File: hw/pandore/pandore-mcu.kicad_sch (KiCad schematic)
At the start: 17 parts, among them U3 RP2350B, U5 mem_flash_spi

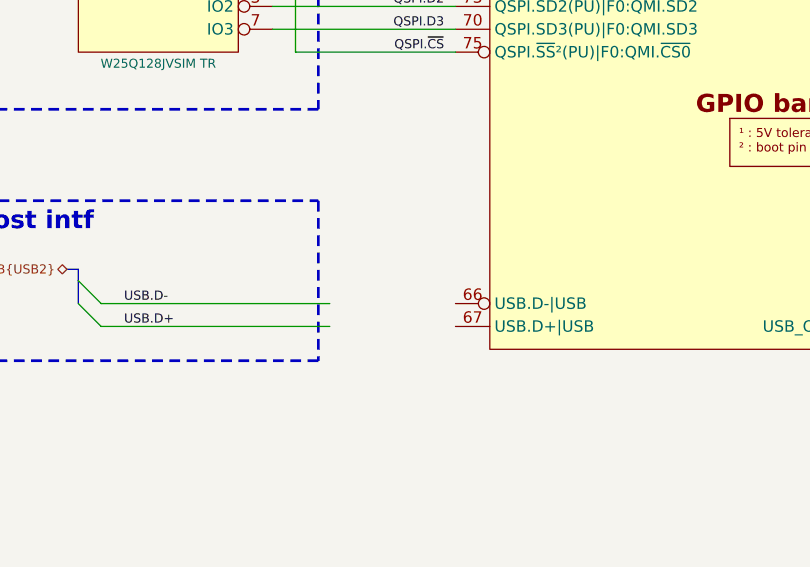
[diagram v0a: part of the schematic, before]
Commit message: added usb, hdmi and combo xlrtrs connectors resized pcb for something realistic (still wip)
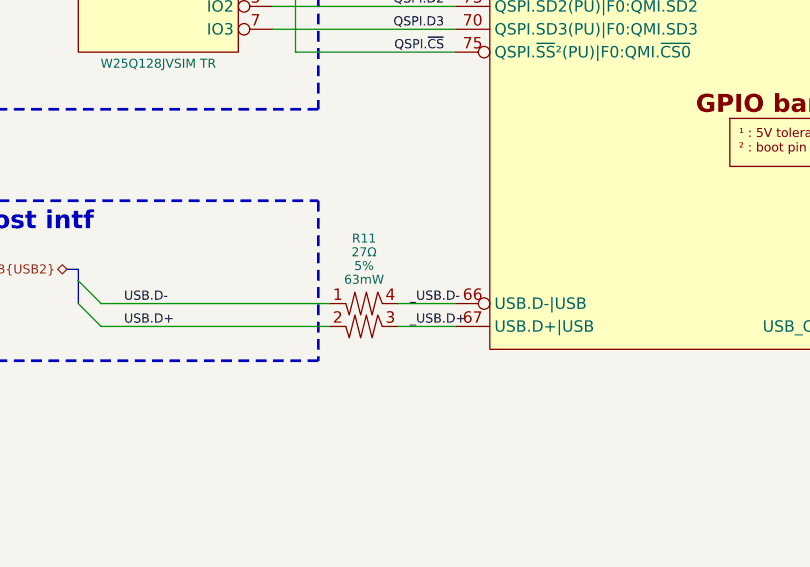
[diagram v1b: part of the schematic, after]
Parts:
- added R11: ${Resistance}, ${Tolerance}, ${Power}, reekilib_res:RESCAXSR65P100X100X35-4, symbol reekilib_res:res_2
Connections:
- net USB.D+: now also R11.2
- net USB.D-: now also R11.1
- net _USB.D-: now reaches U3.66 (USB.D-|USB)
- net _USB.D-: now also R11.4
- net _USB.D+: now reaches U3.67 (USB.D+|USB)
- net _USB.D+: now also R11.3

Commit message: added RP2350's crystals added 8p8c shielded with led connector (both the same for now)
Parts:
- added X1: ${F}, ${tol}+${stab}, ${load}, reekilib_osc:OSCCC320X250X90, symbol reekilib_xtl:crystal_shield
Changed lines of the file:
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@@
+	)
+	(symbol
+		(lib_id "reekilib_xtl:crystal_shield")
+		(at 142.24 43.18 0)
+		(unit 1)
+		(exclude_from_sim no)
+		(in_bom yes)
+		(on_board yes)
+		(dnp no)
+		(property "Reference" "X1"
+			(at 142.24 38.1 0)
+			(do_not_autoplace yes)
+			(effects
+				(font
+					(size 1 1)
+				)
+			)
+		)
+		(property "Value" "${F}, ${tol}+${stab}, ${load}"
+			(at 142.24 38.1 0)
+			(do_not_autoplace yes)
+			(effects
+				(font
+					(size 1 1)
+				)
+				(hide yes)
+			)
+		)
+		(property "Footprint" "reekilib_osc:OSCCC320X250X90"
+			(at 142.24 56.515 0)
+			(do_not_autoplace yes)
+			(effects
+				(font
+					(size 1 1)
+				)
+				(hide yes)
+			)
+		)
+		(property "Datasheet" "https://abracon.com/datasheets/ABM8-272-T3.pdf"
+			(at 142.24 58.42 0)
+			(do_not_autoplace yes)
+			(effects
+				(font
+					(size 1 1)
+				)
+				(hide yes)
+			)
+		)
+		(property "Description" "Crystal with shield"
+			(at 142.24 54.61 0)
+			(do_not_autoplace yes)
+			(effects
+				(font
+					(size 1 1)
+				)
+				(hide yes)
+			)
+		)
+		(property "F" "12MHz"
+			(at 140.97 50.165 0)
+			(do_not_autoplace yes)
+			(effects
+				(font
+					(size 1 1)
+				)
+				(justify right)
+			)
+		)
+		(property "tol" "30ppm"
+			(at 143.51 50.165 0)
+			(do_not_autoplace yes)
+			(effects
+				(font
+					(size 1 1)
+				)
+				(justify left)
+			)
+		)
+		(property "stab" "30ppm"
+			(at 150.495 50.165 0)
+			(do_not_autoplace yes)
+			(effects
+				(font
+					(size 1 1)
+				)
+				(justify left)
+				(hide yes)
+			)
+		)
+		(property "load" "10pF"
+			(at 142.24 52.07 0)
+			(do_not_autoplace yes)
+			(effects
+				(font
+					(size 1 1)
+				)
+			)
+		)
+		(property "MPN" "ABM8-272-T3"
+			(at 142.875 62.23 0)
+			(do_not_autoplace yes)
+			(effects
+				(font
+					(size 1 1)
+				)
+				(hide yes)
+			)
+		)
+		(property "MFG" "Abracon LLC"
+			(at 161.29 62.23 0)
+			(do_not_autoplace yes)
+			(effects
+				(font
+					(size 1 1)
+				)
+				(justify left)
+				(hide yes)
+			)
+		)
+		(property "Link" "https://abracon.com/search?q=ABM8-272-T3"
+			(at 196.215 62.23 0)
+			(do_not_autoplace yes)
+			(effects
+				(font
+					(size 1 1)
+				)
+				(justify left)
+				(hide yes)
+			)
+		)
+		(pin "1"
+		)
+		(pin "3"
+		)
+		(pin "2"
+		)
+		(pin "4"
+		)
+		(instances
+			(project ""
+				(path "/e55f2700-f75a-4062-8a27-fe258faa8966/57ec90ce-deb5-4a52-b1c0-0a997012959b/d2a190b7-8486-4aae-97c0-33ac8d90da8a"
+					(reference "X1")
+					(unit 1)
+				)
+				(path "/e55f2700-f75a-4062-8a27-fe258faa8966/f774142b-755f-468a-93e0-eecae9257f8f/8e05de8b-3536-4686-b4df-144081dee611"
+					(reference "X2")
+					(unit 1)
+				)
+			)
+		)
 	)
 	(symbol

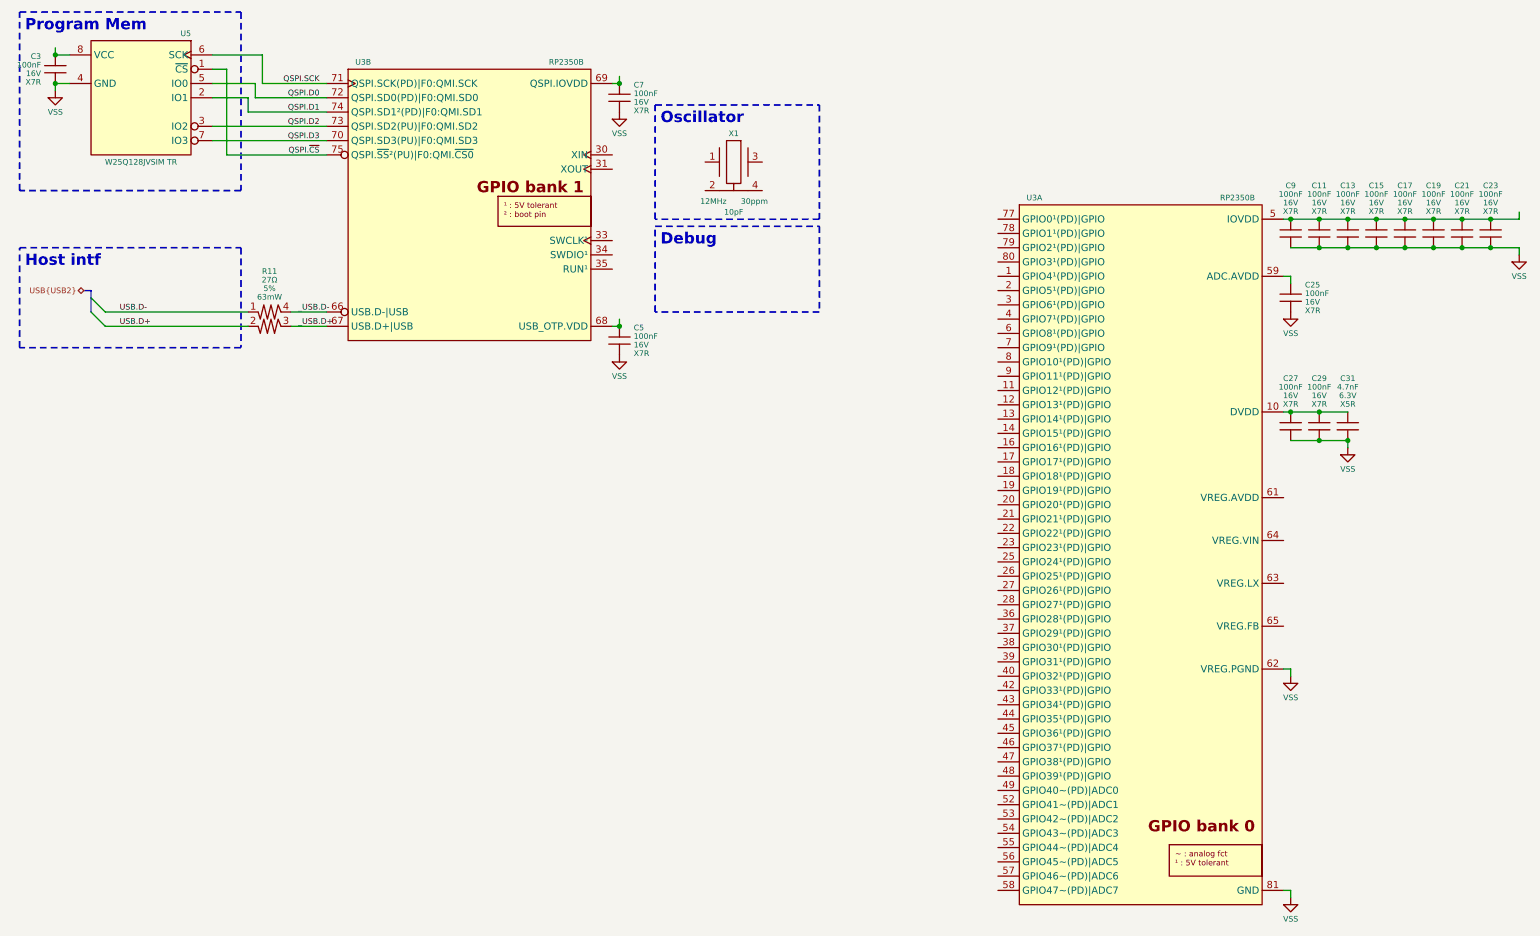
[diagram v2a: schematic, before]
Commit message: Added lots to sch and pcb: eth passive, audio codec, midi, teensy Corrected and added support for M.2
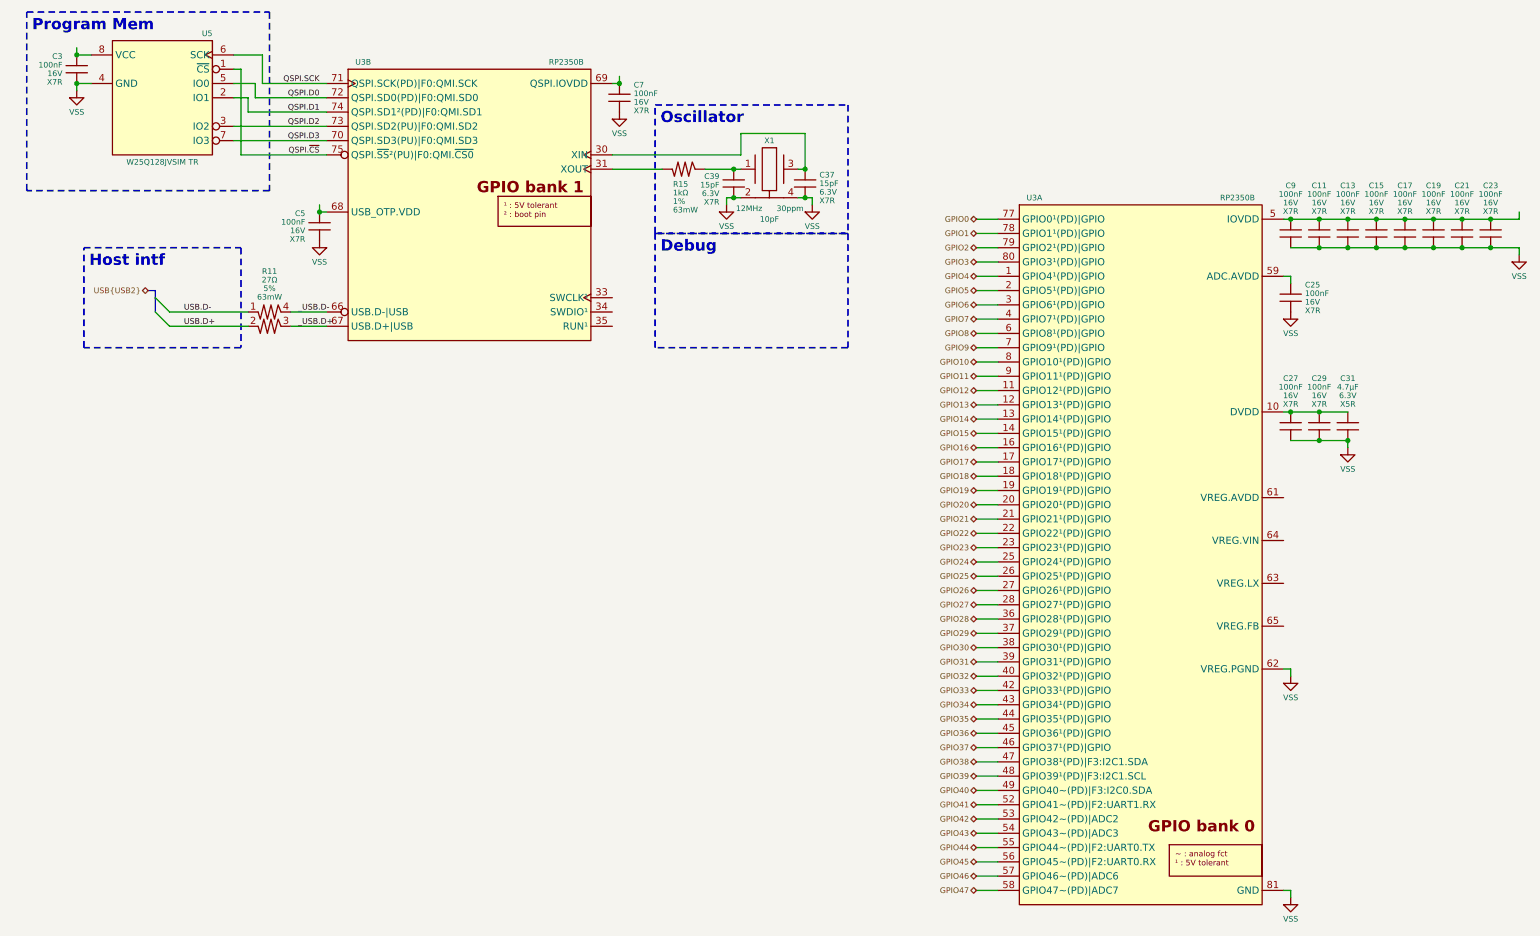
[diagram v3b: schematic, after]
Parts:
- added C37, C39: ${Capacitance}, ${Voltage}, ${Dielectric}, reekilib_cap:CAPC1005, symbol reekilib_cap:cap
- added R15: ${Resistance}, ${Tolerance}, ${Power}, reekilib_res:RESC1005, symbol reekilib_res:res
- C31: Capacitance 4.7nF -> 4.7µF
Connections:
- net VSS: now also X1.2, X1.4, C37.1, C39.1
- net GPIO4: now reaches U3.1 (GPIO4¹(PD)|GPIO)
- net GPIO12: now reaches U3.11 (GPIO12¹(PD)|GPIO)
- net GPIO13: now reaches U3.12 (GPIO13¹(PD)|GPIO)
- net GPIO14: now reaches U3.13 (GPIO14¹(PD)|GPIO)
- net GPIO15: now reaches U3.14 (GPIO15¹(PD)|GPIO)
- net GPIO16: now reaches U3.16 (GPIO16¹(PD)|GPIO)
- net GPIO17: now reaches U3.17 (GPIO17¹(PD)|GPIO)
- net GPIO18: now reaches U3.18 (GPIO18¹(PD)|GPIO)
- net GPIO19: now reaches U3.19 (GPIO19¹(PD)|GPIO)
- net GPIO5: now reaches U3.2 (GPIO5¹(PD)|GPIO)
- net GPIO20: now reaches U3.20 (GPIO20¹(PD)|GPIO)
- net GPIO21: now reaches U3.21 (GPIO21¹(PD)|GPIO)
- net GPIO22: now reaches U3.22 (GPIO22¹(PD)|GPIO)
- net GPIO23: now reaches U3.23 (GPIO23¹(PD)|GPIO)
- net GPIO24: now reaches U3.25 (GPIO24¹(PD)|GPIO)
- net GPIO25: now reaches U3.26 (GPIO25¹(PD)|GPIO)
- net GPIO26: now reaches U3.27 (GPIO26¹(PD)|GPIO)
- net GPIO27: now reaches U3.28 (GPIO27¹(PD)|GPIO)
- net GPIO6: now reaches U3.3 (GPIO6¹(PD)|GPIO)
- net GPIO28: now reaches U3.36 (GPIO28¹(PD)|GPIO)
- net GPIO29: now reaches U3.37 (GPIO29¹(PD)|GPIO)
- net GPIO30: now reaches U3.38 (GPIO30¹(PD)|GPIO)
- net GPIO31: now reaches U3.39 (GPIO31¹(PD)|GPIO)
- net GPIO7: now reaches U3.4 (GPIO7¹(PD)|GPIO)
- net GPIO32: now reaches U3.40 (GPIO32¹(PD)|GPIO)
- net GPIO33: now reaches U3.42 (GPIO33¹(PD)|GPIO)
- net GPIO34: now reaches U3.43 (GPIO34¹(PD)|GPIO)
- net GPIO35: now reaches U3.44 (GPIO35¹(PD)|GPIO)
- net GPIO36: now reaches U3.45 (GPIO36¹(PD)|GPIO)
- net GPIO37: now reaches U3.46 (GPIO37¹(PD)|GPIO)
- net GPIO38: now reaches U3.47 (GPIO38¹(PD)|GPIO)
- net GPIO39: now reaches U3.48 (GPIO39¹(PD)|GPIO)
- net GPIO40: now reaches U3.49 (GPIO40~(PD)|ADC0)
- net GPIO41: now reaches U3.52 (GPIO41~(PD)|ADC1)
- net GPIO42: now reaches U3.53 (GPIO42~(PD)|ADC2)
- net GPIO43: now reaches U3.54 (GPIO43~(PD)|ADC3)
- net GPIO44: now reaches U3.55 (GPIO44~(PD)|ADC4)
- net GPIO45: now reaches U3.56 (GPIO45~(PD)|ADC5)
- net GPIO46: now reaches U3.57 (GPIO46~(PD)|ADC6)
- net GPIO47: now reaches U3.58 (GPIO47~(PD)|ADC7)
- net GPIO8: now reaches U3.6 (GPIO8¹(PD)|GPIO)
- net GPIO9: now reaches U3.7 (GPIO9¹(PD)|GPIO)
- net GPIO0: now reaches U3.77 (GPIO0¹(PD)|GPIO)
- net GPIO1: now reaches U3.78 (GPIO1¹(PD)|GPIO)
- net GPIO2: now reaches U3.79 (GPIO2¹(PD)|GPIO)
- net GPIO10: now reaches U3.8 (GPIO10¹(PD)|GPIO)
- net GPIO3: now reaches U3.80 (GPIO3¹(PD)|GPIO)
- net GPIO11: now reaches U3.9 (GPIO11¹(PD)|GPIO)
- net at U3.30 (XIN): now also X1.3, C37.2
- net at U3.31 (XOUT): now also R15.1
- net at X1.1: now also C39.2, R15.2
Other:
- moved on the sheet: C3, C5, U5, X1

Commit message: Lots of routing done power blocks intra-routing mostly done rp2350 routing mostly done some label cleanup
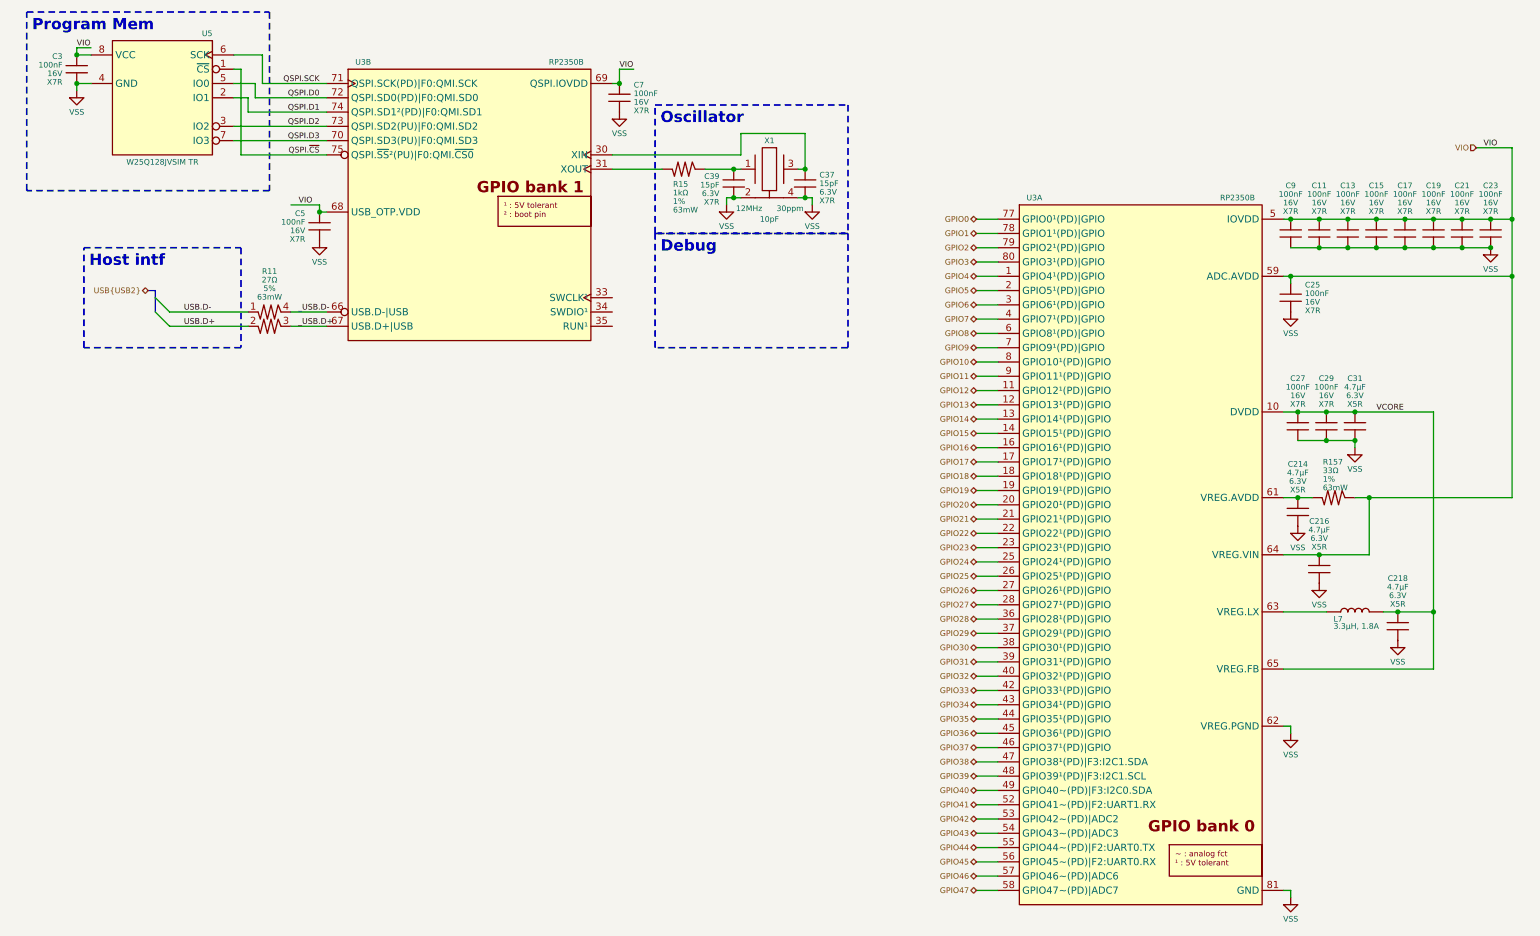
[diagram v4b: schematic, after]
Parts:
- added C214, C216, C218: ${Capacitance}, ${Voltage}, ${Dielectric}, reekilib_cap:CAPC1005, symbol reekilib_cap:cap
- added L7: 3.3µH, 1.8A, reekilib_ind:INDC2012, symbol reekilib_ind:ind
- added R157: ${Resistance}, ${Tolerance}, ${Power}, reekilib_res:RESC1005, symbol reekilib_res:res
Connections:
- net VSS: now also C214.1, C216.1, C218.1
- net VIO: now reaches C11.2, C13.2, C15.2, C17.2, C19.2, C21.2, C23.2, C9.2, U3.15 (IOVDD), U3.24 (IOVDD), U3.29 (IOVDD), U3.41 (IOVDD), U3.5 (IOVDD), U3.50 (IOVDD), U3.60 (IOVDD), U3.76 (IOVDD)
- net VIO: now also C25.2, C3.2, C5.2, C7.2, U3.59 (ADC.AVDD), U3.64 (VREG.VIN), U3.68 (USB_OTP.VDD), U3.69 (QSPI.IOVDD), U5.8 (VCC), C216.2, R157.2
- net VCORE: now reaches C27.2, C29.2, C31.2, U3.10 (DVDD), U3.32 (DVDD), U3.51 (DVDD)
- net VCORE: now also U3.65 (VREG.FB), C218.2, L7.2
- net at U3.61 (VREG.AVDD): now also C214.2, R157.1
- net at U3.63 (VREG.LX): now also L7.1
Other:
- moved on the sheet: C27, C29, C31

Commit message: most of board control signals added, routed and defined
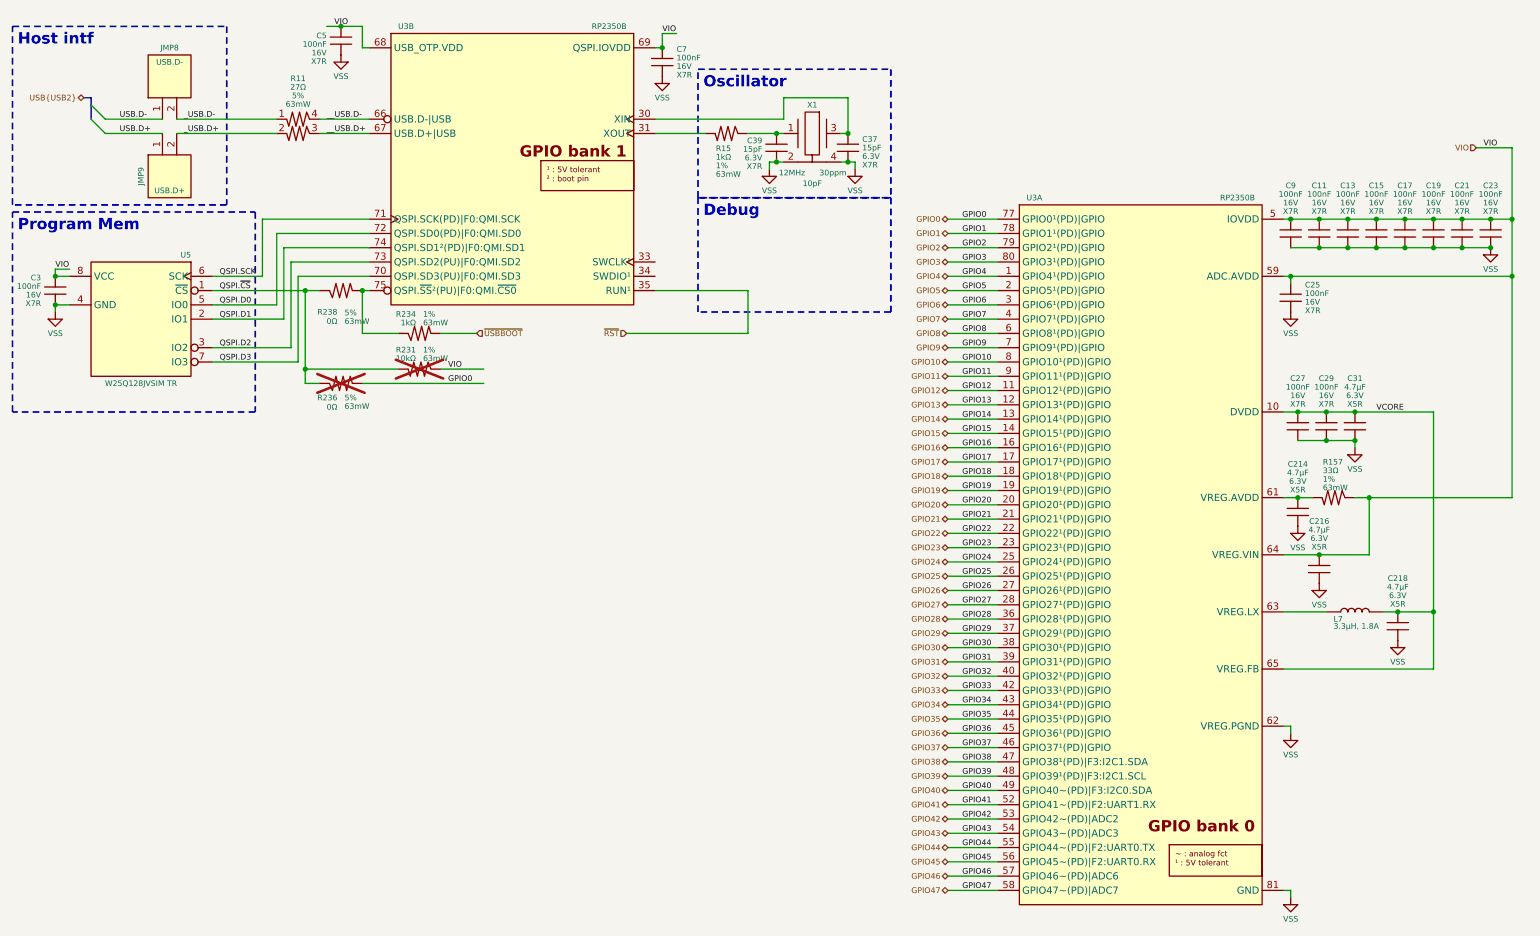
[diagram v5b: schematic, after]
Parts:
- added JMP8: USB.D-, reekilib_con:HDR254P1X02-TH, symbol reekilib_con:hdr-1x2
- added JMP9: USB.D+, reekilib_con:HDR254P1X02-TH, symbol reekilib_con:hdr-1x2
- added R231, R234, R236, R238: ${Resistance}, ${Tolerance}, ${Power}, reekilib_res:RESC1005, symbol reekilib_res:res
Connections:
- net GPIO0: now also R236.1
- net QSPI.~{CS}: now also R231.1, R236.2, R238.2; no longer U3.75 (QSPI.~{SS}²(PU)|F0:QMI.~{CS0})
- net USB.D+: now also JMP9.1; no longer R11.2
- net USB.D-: now also JMP8.1; no longer R11.1
- net VIO: now also R231.2
- net _USB.D+: now also R11.2, JMP9.2; no longer R11.3, U3.67 (USB.D+|USB)
- net _USB.D-: now also R11.1, JMP8.2; no longer R11.4, U3.66 (USB.D-|USB)
- net ~{RST}: now reaches U3.35 (RUN¹)
- new net: R234.2, R238.1, U3.75 (QSPI.~{SS}²(PU)|F0:QMI.~{CS0})
- new net __USB.D+: R11.3, U3.67 (USB.D+|USB)
- new net __USB.D-: R11.4, U3.66 (USB.D-|USB)
- new net ~{USBBOOT}: R234.1
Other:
- moved on the sheet: C3, C37, C39, C5, C7, R11, R15, U3B, U5, X1
